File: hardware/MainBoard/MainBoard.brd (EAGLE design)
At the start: 90 x 56 mm, 269 parts, among them J1 CON-71741-2184-BOT, J2 CON-71741-2184-TOP, J3 CON-FTSH-105-01-L-DV-K, J4 CON-ZX62R-B-5P, J7 CON-RJ45-J0G-0007NL, J8 SWITCH-CJS-1200-1200, M1 MOUNT-HOLE3.3, M2 MOUNT-HOLE3.3, M3 MOUNT-HOLE3.3, M4 MOUNT-HOLE3.3, M5 FIDUCIAL1X2, M6 FIDUCIAL1X2, M7 FIDUCIAL1X2, M8 FIDUCIAL1X2, Q1 MMBT3904, SW1 SWITCH-ESWITCH-TL3340G, SW2 SWITCH-ESWITCH-TL3340G, U1 A2F500M3G-1FGG256, U2 MAX19706-T4877-4, U3 MAX19706-T4877-4, U4 USBLC6-2SC6, U5 FT232HL, U6 DP83848C-VBH48A, U7 93LC56BT-OT, U8 DS1818-10-SOT-23, X1 ECX-2236-200, X2 ECX-31B, X3 ASEM1-C, X5 ECX-42-120

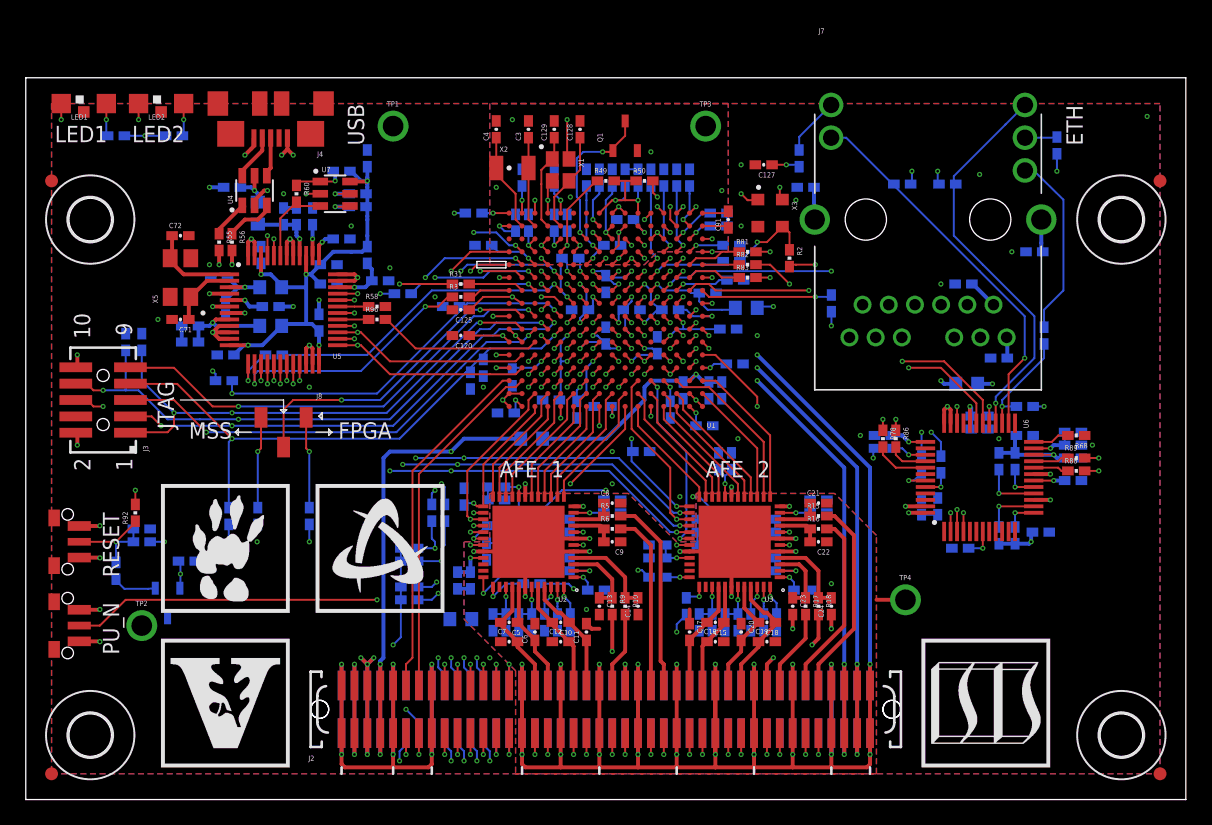
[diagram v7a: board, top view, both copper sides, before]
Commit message: Re-numbered components based on schematic page/location.
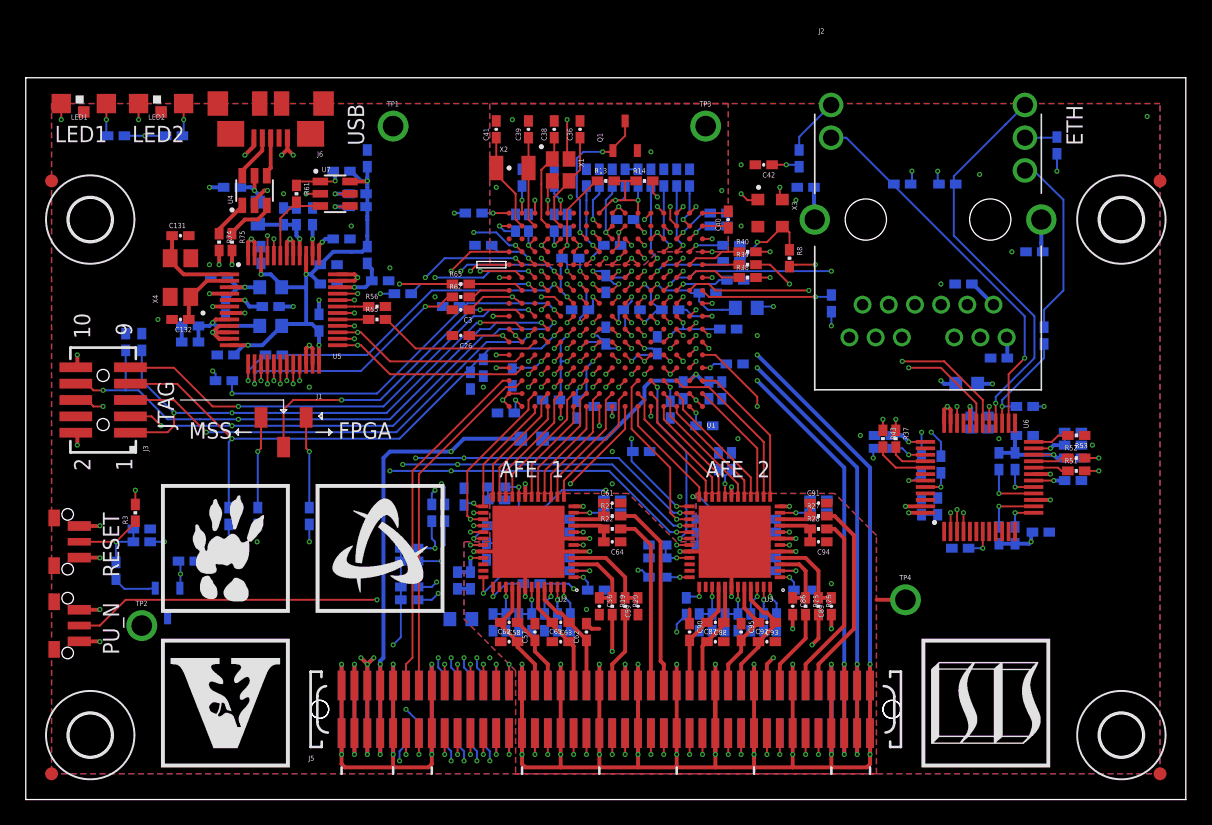
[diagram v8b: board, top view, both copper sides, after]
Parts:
- removed J7: CON-RJ45-J0G-0007NL, MainBoard:J0G-0007NL
- removed J8: SWITCH-CJS-1200-1200, MainBoard:SWITCH-DIP-CJS
- removed R84: 1.5k, MainBoard:R0402
- removed R88, R89: 2.2k, MainBoard:R0402
- removed R91, R94: 10k, MainBoard:R0402
- removed R92: 39, MainBoard:R0402
- removed R93: 0, MainBoard:R0402
- removed R96: 27, MainBoard:R0402
- removed R97, R98: (no value), MainBoard:R0402
- added J5: CON-71741-2184-TOP, MainBoard:71741-0002
- added J6: CON-ZX62R-B-5P, MainBoard:ZX62R-B-5P
- added R20: 24.9, MainBoard:R0402
- added R24: 100k, MainBoard:R0402
- added R32, R42: 110, MainBoard:R0402
- added R34, R35, R36: 49.9, MainBoard:R0402
- added R46, R47, R48: 2.2k, MainBoard:R0402
- C1, C70: value (none) -> 2.2uF
- C10, C11, C12, C15, C16, C17, C18, C19, C2, C20, C5, C6, C69, C7: value (none) -> 0.1uF
- C100: value 4.7uF -> 2.2uF
- C102, C104, C114, C74, C78, C80, C84: value 0.1uF -> 2.2uF
- C106: value 10nF -> 2.2uF
- C108: value 1000pF -> 2.2uF
- C109, C26, C28, C30, C32: value 2.2uF -> 0.1uF
- C110, C112, C82: value 10uF -> 2.2uF
- C111: value 10uF -> 0.1uF
- C116: value 10uF -> 1000pF
- C117: value 0.1uF -> 1000pF
- C118: value 0.01uF -> 0.1uF
- C123, C27, C49, C51: value 0.1uF -> 10uF
- C127: value 0.01uF -> 10uF
- C128, C71: value 10pF -> 0.1uF
- C129: value 10pF -> 10uF
- C13, C14, C21, C22, C23, C24, C8, C9: value 22pF -> 0.1uF
- C131, C132: value 0.1uF -> 10pF
- C133, C135: value 0.1uF -> 10nF
- C136, C138, C140, C142: value 0.1uF -> 4.7uF
- C148: value 1000pF -> 0.1uF
- C25, C43, C75: value 0.33uF -> 0.1uF
- C29: value 0.1uF -> 0.01uF
- C3, C4: value 4pF -> 0.1uF
- C34, C48, C52, C54, C58, C60: value 2.2uF -> (none)
- C35, C37, C47, C53, C55, C57, C87, C95: value 0.1uF -> (none)
- C36, C38: value 2.2uF -> 10pF
- C39, C41: value 0.1uF -> 4pF
- C40: value 2.2uF -> 2.2u
- C42: value 0.33uF -> 0.01uF
- C46: value 2.2uF -> 0.01uF
- C50: value 2.2uF -> 10uF
- C56: value 2.2uF -> 22pF
- C59, C61, C64, C89, C94: value 0.1uF -> 22pF
- C62, C63: value 0.33uF -> (none)
- C66, C67, C68: value (none) -> 0.33uF
- C72: value 10pF -> 2.2uF
- C76: value 0.01uF -> 2.2uF
- C86: value 10uF -> 22pF
- C88: value 10uF -> (none)
- C91: value 2.2u -> 22pF
- C92: value 10nF -> (none)
- C93: value 4.7uF -> (none)
- C96, C98: value 4.7uF -> 0.33uF
- C97: value 0.1uF -> 0.33uF
- J1: value CON-71741-2184-BOT -> SWITCH-CJS-1200-1200; device MainBoard:71742-3003-BOT -> MainBoard:SWITCH-DIP-CJS
- J2: value CON-71741-2184-TOP -> CON-RJ45-J0G-0007NL; device MainBoard:71741-0002 -> MainBoard:J0G-0007NL
- J4: value CON-ZX62R-B-5P -> CON-71741-2184-BOT; device MainBoard:ZX62R-B-5P -> MainBoard:71742-3003-BOT
- LOGO1: value LOGO-ISIS-600MIL-10MM-SS -> LOGO-VANDERBILT-600MIL-10MM-SS; device Logo:LOGO-ISIS-10MM-SILKSCREEN -> Logo:LOGO-VANDERBILT-10MM-SILKSCREEN
- LOGO2: value LOGO-VANDERBILT-600MIL-10MM-SS -> LOGO-ISIS-600MIL-10MM-SS; device Logo:LOGO-VANDERBILT-10MM-SILKSCREEN -> Logo:LOGO-ISIS-10MM-SILKSCREEN
- R1, R2: value 39 -> 10k
- R10, R5, R6, R9: value 24.9 -> 1k
- R11: value 100k -> 0
- R12: value 2.2k -> 0
- R13: device MainBoard:R0603 -> MainBoard:R0402
- R14: value 100 -> 0
- R15, R16, R17, R18: value 24.9 -> 0
- R19, R21, R22, R25: value 100k -> 24.9
- R26: value 0 -> 24.9
- R27: value 100 -> 24.9
- R28: value 4.7k -> 24.9
- R29: value 4.7k -> 100k
- R30: value 39 -> 100k
- R31: value 39 -> 1.5k
- R4: value 39 -> 0
- R50, R51, R52: value 0 -> 2.2k
- R53: value 0 -> 4.87k
- R54: value 0 -> 12k
- R55: value 0 -> 27
- R56: value 0 -> 39k
- R58: value 39k -> 10k
- R59: value 12k -> 10k
- R60: value 2k -> 10k
- R61: value 10k -> 2k
- R62, R63: value 10k -> 39
- R64, R65: value 1k -> 39
- R66, R67: value 1k -> (none)
- R68: value 4.87k -> 100k
- R69: value 110 -> 100k
- R7, R8: value 0 -> 39
- R70: value 110 -> 4.7k
- R71: value 2.2k -> 4.7k
- R72, R73: value 2.2k -> 100
- R74, R75: value 49.9 -> 0
- R76: value 49.9 -> 0; device MainBoard:R0402 -> MainBoard:R0603
- moved R74 64.0 mm to (15.0, 43.2), flipped to the top, turned to 270 degrees
- moved C130 62.5 mm to (74.0, 29.8)
- moved R75 61.9 mm to (16.0, 43.2), flipped to the top, turned to 270 degrees
- moved R69 60.8 mm to (29.8, 16.5), turned to 0 degrees
- moved LOGO1 59.0 mm to (10.5, 2.50)
- moved LOGO2 59.0 mm to (69.5, 2.50)
- moved R12 56.8 mm to (15.8, 22.0), turned to 270 degrees
- moved R2 54.9 mm to (9.00, 20.0), flipped to the bottom, turned to 180 degrees
- moved C92 54.5 mm to (57.5, 12.2), flipped to the top
- moved J4 53.7 mm to (45.0, 7.00), flipped to the bottom
- moved R68 53.3 mm to (29.8, 15.5), flipped to the bottom, turned to 0 degrees
- moved C97 50.9 mm to (58.2, 13.8), turned to 270 degrees
- moved C96 49.9 mm to (60.2, 16.2), turned to 180 degrees
- moved C98 49.5 mm to (57.2, 13.8), turned to 270 degrees
- moved C125 49.3 mm to (81.2, 24.8), flipped to the bottom
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- renumbered R77 to R33, R78 to R43, R79 to R44, R80 to R45, R81 to R40, R82 to R39, R83 to R38, R85 to R41, R86 to R37, R95 to R57, X5 to X4
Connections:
- net !AFE1_SHDN: now also R24.2; no longer R19.2
- net !AFE2_SHDN: now also R30.2; no longer R23.2
- net !MSS_RESET: now also R3.2; no longer R92.2
- net !MSS_RESET_PB: now also C37.1, R2.1, R3.1, R4.2, SW2.2; no longer C90.1, R91.1, R92.1, R93.2, SW1.2
- net !PWRSAV: now also R56.1; no longer R58.1
- net !SPI1_SS_AFE1: now also R23.1; no longer R22.1
- net !SPI1_SS_AFE2: now also R29.1; no longer R25.1
- net !USB_RESET: now also C133.1; no longer C106.1
- net !WAKEUP: now also J4.27, J5.27, R1.2, SW1.2; no longer J1.27, J2.27, R94.2, SW2.2
- net A1V5: now also C34.1, C35.1, J4.79, J4.80, J5.79, J5.80; no longer C1.1, C2.1, J1.79, J1.80, J2.79, J2.80
- net A3V3: now also C100.1, C101.1, C102.1, C103.1, C104.1, C105.1, C106.1, C107.1, C108.1, C109.1, C110.1, C111.1, C112.1, C113.1, C19.1, C20.1, C21.1, C22.1, C23.1, C24.1, C25.1, C69.1, C70.1, C71.1, C72.1, C73.1, C74.1, C75.1, C76.1, C77.1, C78.1, C79.1, C80.1, C81.1, C82.1, C83.1, C99.1, J4.81, J4.82, J5.81, J5.82, R14.2; no longer C119.1, C121.1, C122.1, C123.1, C124.1, C132.1, C133.1, C26.1, C27.1, C28.1, C29.1, C30.1, C31.1, C32.1, C33.1, C34.1, C35.1, C36.1, C37.1, C38.1, C39.1, C44.1, C46.1, C47.1, C48.1, C49.1, C50.1, C51.1, C52.1, C53.1, C54.1, C55.1, C56.1, C57.1, C58.1, C59.1, C64.1, J1.81, J1.82, J2.81, J2.82, R50.2
- net ADC1+: now also J5.46, R19.2; no longer J2.46, R9.2
- net ADC1-: now also J5.44, R20.2; no longer J2.44, R10.2
- net ADC1-IAN: now also C59.2, R20.1; no longer C14.2, R10.1
- net ADC1-IAP: now also C56.1, R19.1; no longer C13.1, R9.1
- net ADC2+: now also J5.52, R21.2; no longer J2.52, R5.2
- net ADC2-: now also J5.50, R22.2; no longer J2.50, R6.2
- net ADC2-QAN: now also C64.2, R22.1; no longer C9.2, R6.1
- net ADC2-QAP: now also C61.1, R21.1; no longer C8.1, R5.1
- net ADC3+: now also J5.70, R25.2; no longer J2.70, R17.2
- net ADC3-: now also J5.68, R26.2; no longer J2.68, R18.2
- net ADC3-IAN: now also C89.2, R26.1; no longer C24.2, R18.1
- net ADC3-IAP: now also C86.1, R25.1; no longer C23.1, R17.1
- net ADC4+: now also J5.76, R27.2; no longer J2.76, R15.2
- net ADC4-: now also J5.74, R28.2; no longer J2.74, R16.2
- net ADC4-QAN: now also C94.2, R28.1; no longer C22.2, R16.1
- net ADC4-QAP: now also C91.1, R27.1; no longer C21.1, R15.1
- net AFE1_COM: now also C68.1; no longer C43.1
- net AFE1_REFN: now also C67.1; no longer C42.1
- net AFE1_REFP: now also C66.1; no longer C25.1
- net AFE2_COM: now also C98.1; no longer C63.1
- net AFE2_REFN: now also C97.1; no longer C62.1
- net AFE2_REFP: now also C96.1; no longer C45.1
- net AGND: now also C100.2, C101.2, C102.2, C103.2, C104.2, C105.2, C106.2, C107.2, C108.2, C113.2, C20.2, C22.2, C24.2, C41.2, C59.1, C60.1, C61.2, C64.1, C65.1, C71.2, C72.2, C73.2, C74.2, C75.2, C76.2, C77.2, C78.2, C79.2, C80.2, C81.2, C82.2, C83.2, C86.2, C87.2, C89.1, C90.1, C91.2, C92.2, C94.1, C95.1, C96.2, C97.2, C98.2, C99.2, J4.29, J4.30, J4.35, J4.36, J4.41, J4.42, J4.47, J4.48, J4.53, J4.54, J4.59, J4.60, J4.65, J4.66, J4.71, J4.72, J4.77, J4.78, J4.83, J4.84, J5.29, J5.30, J5.35, J5.36, J5.41, J5.42, J5.47, J5.48, J5.53, J5.54, J5.59, J5.60, J5.65, J5.66, J5.71, J5.72, J5.77, J5.78, J5.83, J5.84, R76.2; no longer C11.2, C119.2, C12.1, C121.2, C122.2, C123.2, C124.2, C128.2, C129.2, C13.2, C132.2, C133.2, C14.1, C16.2, C17.1, C2.2, C20.1, C22.1, C24.1, C26.2, C27.2, C28.2, C29.2, C3.2, C30.2, C31.2, C32.2, C33.2, C37.2, C4.2, C42.2, C43.2, C44.2, C45.2, C46.2, C58.2, C59.2, C6.2, C63.2, C64.2, C65.2, C7.1, C8.2, C9.1, J1.29, J1.30, J1.35, J1.36, J1.41, J1.42, J1.47, J1.48, J1.53, J1.54, J1.59, J1.60, J1.65, J1.66, J1.71, J1.72, J1.77, J1.78, J1.83, J1.84, J2.29, J2.30, J2.35, J2.36, J2.41, J2.42, J2.47, J2.48, J2.53, J2.54, J2.59, J2.60, J2.65, J2.66, J2.71, J2.72, J2.77, J2.78, J2.83, J2.84, R13.2
- net ALERT: now also J4.25, J5.25; no longer J1.25, J2.25
- net AUX_DAC1: now also R15.1; no longer R51.1
- net AUX_DAC2: now also R16.1; no longer R52.1
- net AUX_DAC3: now also R17.1; no longer R53.1
- net AUX_DAC4: now also R18.1; no longer R54.1
- net COM+: now also J2.16, R42.1; no longer J7.16, R69.1
- net D1V5: now also C26.1, C30.1, C31.1, C32.1, C33.1, J4.7, J4.8, J5.7, J5.8; no longer C113.1, C114.1, C115.1, C120.1, C73.1, J1.7, J1.8, J2.7, J2.8
- net D3V3: now also C10.1, C11.1, C114.1, C115.1, C12.1, C128.1, C129.1, C13.1, C14.1, C15.1, C16.1, C17.1, C2.1, C3.1, C4.1, C42.1, C43.1, C5.1, C6.1, C7.1, C8.1, C84.1, C85.1, C9.1, J4.5, J4.6, J5.5, J5.6, R1.1, R12.2, R2.2, R23.2, R31.2, R32.2, R42.2, R46.2, R47.2, R48.2, R5.2, R66.2, R68.2; no longer C125.1, C126.1, C134.1, C135.1, C136.1, C137.1, C138.1, C139.1, C140.1, C141.1, C142.1, C143.1, C144.1, C145.1, C146.1, C147.1, C40.1, C41.1, C60.1, C61.1, C86.1, C87.1, C88.1, C89.1, J1.5, J1.6, J2.5, J2.6, R21.2, R22.2, R25.2, R28.2, R7.2, R72.2, R73.2, R8.2, R84.2, R91.2, R94.1, R97.2, R98.2
- net DAC1+: now also C57.1, C58.1, J5.34; no longer C5.1, C6.1, J2.34
- net DAC1-: now also C58.2, C60.2, J5.32; no longer C5.2, C7.2, J2.32
- net DAC2+: now also C62.1, C63.1, J5.40; no longer C10.1, C11.1, J2.40
- net DAC2-: now also C63.2, C65.2, J5.38; no longer C10.2, C12.2, J2.38
- net DAC3+: now also C87.1, C88.1, J5.58; no longer C15.1, C16.1, J2.58
- net DAC3-: now also C88.2, C90.2, J5.56; no longer C15.2, C17.2, J2.56
- net DAC4+: now also C92.1, C93.1, J5.64; no longer C18.1, C19.1, J2.64
- net DAC4-: now also C93.2, C95.2, J5.62; no longer C18.2, C20.2, J2.62
- net DGND: now also C10.2, C11.2, C119.2, C12.2, C121.2, C122.2, C123.2, C124.2, C128.2, C129.2, C13.2, C132.2, C133.2, C14.2, C15.2, C16.2, C17.2, C18.2, C2.2, C26.2, C27.2, C28.2, C29.2, C3.2, C30.2, C31.2, C32.2, C33.2, C37.2, C4.2, C42.2, C43.2, C44.2, C45.2, C46.2, C5.2, C6.2, C7.2, C8.2, C9.2, J4.1, J4.10, J4.15, J4.16, J4.2, J4.9, J5.1, J5.10, J5.15, J5.16, J5.2, J5.9, J6.5, R10.1, R24.1, R30.1, R50.1, R53.1, R54.1, R6.1, R76.1, R9.1; no longer C100.2, C101.2, C102.2, C103.2, C104.2, C105.2, C106.2, C107.2, C108.2, C113.2, C40.2, C41.2, C60.2, C61.2, C71.2, C72.2, C73.2, C74.2, C75.2, C76.2, C77.2, C78.2, C79.2, C80.2, C81.2, C82.2, C83.2, C86.2, C87.2, C88.2, C89.2, C90.2, C92.2, C93.2, C94.2, C95.2, C96.2, C97.2, C98.2, C99.2, J1.1, J1.10, J1.15, J1.16, J1.2, J1.9, J2.1, J2.10, J2.15, J2.16, J2.2, J2.9, J4.5, R12.1, R13.1, R19.1, R23.1, R59.1, R64.1, R65.1, R66.1, R68.1
- net E3V3: now also C118.1, C119.1, C120.1, C121.1, C122.1, J2.12, J2.6, R34.2, R35.2, R36.2, R51.2, R52.2; no longer C77.1, C78.1, C79.1, C80.1, C81.1, J7.12, J7.6, R74.2, R75.2, R76.2, R88.2, R89.2
- net EECLK: now also R59.1; no longer R62.1
- net EECS: now also R60.1; no longer R63.1
- net EEDATA: now also R61.2; no longer R60.2
- net EEDO: now also R58.1; no longer R60.1
- net ETH-RBIAS: now also R53.2; no longer R68.2
- net EXTIC-RST: now also R4.1; no longer R93.1
- net FPGATAP: now also J1.1, R5.1; no longer J8.1, R67.1
- net I2C0_SCL: now also J4.26, J5.26, R70.1, R72.2; no longer J1.26, J2.26, R27.2, R29.1
- net I2C0_SCLI: now also R72.1; no longer R27.1
- net I2C0_SDA: now also J4.28, J5.28, R71.1, R73.2; no longer J1.28, J2.28, R14.2, R28.1
- net I2C0_SDAI: now also R73.1; no longer R14.1
- net JTAGSEL: now also J1.2; no longer J8.2
- net LED1H: now also R66.1; no longer R97.1
- net LED2H: now also R67.1; no longer R98.1
- net LED_ETH_ACT: now also J2.13, R48.1; no longer J7.13, R71.1
- net LED_ETH_LINK: now also J2.17, R46.1; no longer J7.17, R73.1
- net LED_ETH_SPD: now also J2.15, R49.2; no longer J7.15, R26.2
- net LED_PHY_SPEED: now also R47.1, R49.1; no longer R26.1, R72.1
- net LPXIN: now also C39.1; no longer C3.1
- net LPXOUT: now also C41.1; no longer C4.1
- net MAC_EN: now also R50.2; no longer R12.2
- net MAC_MDIO: now also R31.1; no longer R84.1
- net MAC_RMII_CLK: now also R7.2; no longer R1.2
- net MAINXIN: now also C36.1; no longer C128.1
- net MAINXOUT: now also C38.1; no longer C129.1
- net MSSTAP: now also J1.3, R6.2; no longer J8.3, R66.2
- net NCAP: now also C40.2; no longer C91.2
- net NGPIO0: now also J5.11; no longer J2.11
- net NGPIO1: now also J5.13; no longer J2.13
- net NGPIO2: now also J5.17; no longer J2.17
- net NGPIO3: now also J5.19; no longer J2.19
- net PCAP: now also C40.1; no longer C91.1
- net PFBOUT: now also C123.1, C124.1, C125.1, C126.1; no longer C82.1, C83.1, C84.1, C85.1
- net PHY_RMII_CLK: now also R8.2; no longer R2.2
- net RD+: now also J2.4, R34.1; no longer J7.4, R76.1
- net RD-: now also J2.5; no longer J7.5
- net REF_CLK+: now also J5.14; no longer J2.14
- net REF_CLK-: now also J5.12; no longer J2.12
- net RJ45-CHS-1: now also C116.1, J2.H$1; no longer C148.1, J7.H$1
- net RJ45-CHS-2: now also C117.1, J2.H$2; no longer C108.1, J7.H$2
- net RMII_CLK: now also R7.1, R8.1; no longer R1.1, R2.1
- net RSVD-P20: now also R51.1; no longer R88.1
- net RSVD-P21: now also R52.1; no longer R89.1
- net SF_ABPS0: now also J5.75; no longer J2.75
- net SF_ABPS1: now also J5.73; no longer J2.73
- net SF_ADC0: now also J5.49; no longer J2.49
- net SF_ADC1: now also C55.1, J5.51, R18.2; no longer C67.1, J2.51, R54.2
- net SF_ADC2: now also J5.55; no longer J2.55
- net SF_ADC3: now also C54.1, J5.57, R17.2; no longer C68.1, J2.57, R53.2
- net SF_ADC4: now also J5.45; no longer J2.45
- net SF_ADC5: now also C53.1, J5.43, R16.2; no longer C69.1, J2.43, R52.2
- net SF_ADC6: now also J5.39; no longer J2.39
- net SF_ADC7: now also C52.1, J5.37, R15.2; no longer C70.1, J2.37, R51.2
- net SF_CM0: now also J5.69; no longer J2.69
- net SF_CM1: now also J5.63; no longer J2.63
- net SF_DAC0: now also C47.1, J5.33; no longer C66.1, J2.33
- net SF_DAC1: now also C48.1, J5.31; no longer C65.1, J2.31
- net SF_TM0: now also J5.67; no longer J2.67
- net SF_TM1: now also J5.61; no longer J2.61
- net SGPIO0: now also J4.11; no longer J1.11
- net SGPIO1: now also J4.13; no longer J1.13
- net SGPIO2: now also J4.17; no longer J1.17
- net SGPIO3: now also J4.19; no longer J1.19
- net SGPIO4: now also J4.21; no longer J1.21
- net SGPIO5: now also J4.23; no longer J1.23
- net SPI0_MISO: now also J4.22; no longer J1.22
- net SPI0_MOSI: now also J4.20; no longer J1.20
- net SPI0_SCLK: now also J4.18; no longer J1.18
- net SPI0_SS: now also J4.24, R68.1; no longer J1.24, R11.1
- net SPI1_MISO: now also J5.22; no longer J2.22
- net SPI1_MOSI: now also J5.20; no longer J2.20
- net SPI1_SCLK: now also J5.18; no longer J2.18
- net SPI1_SS: now also J5.24, R69.1; no longer J2.24, R21.1
- net TCK: now also R10.2; no longer R65.2
- net TD+: now also J2.11, R36.1; no longer J7.11, R74.1
- net TD-: now also J2.10, R35.1; no longer J7.10, R75.1
- net TRST: now also R9.2; no longer R64.2
- net U3V3: now also C142.1, C143.1, C145.1, C146.1, C147.1, C148.1, R58.2, R59.2, R60.2; no longer C100.1, C101.1, C102.1, C103.1, C104.1, C105.1, R61.2, R62.2, R63.2
- net UART0_RXD: now also R63.2; no longer R4.2
- net UART0_TXD: now also R62.2; no longer R3.2
- net UART1_RXD: now also J5.23, R65.1; no longer J2.23, R31.1
- net UART1_RXDI: now also R65.2; no longer R31.2
- net UART1_TXD: now also J5.21, R64.1; no longer J2.21, R30.1
- net UART1_TXDI: now also R64.2; no longer R30.2
- net UREF: now also R54.2; no longer R59.2
- net USBDM: now also R74.2; no longer R55.2
- net USBDM-IN: now also J6.2; no longer J4.2
- net USBDM-OUT: now also R74.1; no longer R55.1
- net USBDP: now also R75.2; no longer R56.2
- net USBDP-IN: now also J6.3; no longer J4.3
- net USBDP-OUT: now also R75.1; no longer R56.1
- net USB_CLK: now also R55.2; no longer R96.2
- net USB_CLKF: now also R55.1; no longer R96.1
- net USB_DB0: now also R63.1; no longer R4.1
- net USB_DB1: now also R62.1; no longer R3.1
- net UXCSI: now also C131.1; no longer C72.1
- net UXCSO: now also C132.1; no longer C71.1
- net VAREFIN: now also C50.1, C51.1, R13.2, R14.1; no longer C110.1, C111.1, R49.2, R50.1
- net VAREFOUT: now also C49.1, R13.1; no longer C112.1, R49.1
- net VBAT: now also R56.2; no longer R58.2
- net VBUS: now also C135.1, J6.1; no longer C92.1, J4.1
- net VCC3N: now also C1.1; no longer C109.1
- net VCCA: now also C134.1; no longer C107.1
- net VCCPLL0: now also C27.1, C28.1, C29.1; no longer C116.1, C117.1, C118.1
- net VCCRCOSC: now also C18.1; no longer C131.1
- net VCORE: now also C144.1; no longer C95.1
- net VJTAG: now also C44.1, R11.1; no longer C74.1, R8.1
- net VPHY: now also C138.1, C139.1; no longer C96.1, C97.1
- net VPLL: now also C140.1, C141.1; no longer C98.1, C99.1
- net VPUMP: now also C45.1, C46.1, R12.1; no longer C75.1, C76.1, R7.1
- net VREGIN: now also C136.1, C137.1; no longer C93.1, C94.1
- net VSUP: now also J4.3, J4.4, J5.3, J5.4; no longer J1.3, J1.4, J2.3, J2.4
- net YEL+: now also J2.14, R32.1; no longer J7.14, R70.1
